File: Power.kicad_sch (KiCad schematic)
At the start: 34 parts, among them Q50 DMP3068L-7, SW50 SW_SPST, U50 MCP73831-2-OT, U51 MIC845H, U52 LM66200DRLR, U53 TPS631000DRLR

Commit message: Ground Stitching, PMOS 0-Res Moved,
DRC should be near cleared. Might want to reconsider mapping some pin functions? SD card detect line, also battery checker (making use of comparator). Also, double check if audio IC microphone pins (and ADC) are supposed to be pulled to VMID
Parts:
- C54, C55: footprint Capacitor_SMD:C_0603_1608Metric_Pad1.08x0.95mm_HandSolder -> Capacitor_SMD:C_0805_2012Metric
- TP50, TP52: footprint TestPoint:TestPoint_Pad_1.5x1.5mm -> footprints:TestPoint_Pad_1.5x1.5mm
- TP51: footprint TestPoint:TestPoint_Pad_1.5x1.5mm -> TestPoint:TestPoint_THTPad_1.5x1.5mm_Drill0.7mm
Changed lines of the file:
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@@
 			)
 		)
-		(property "Footprint" "TestPoint:TestPoint_Pad_1.5x1.5mm"
+		(property "Footprint" "footprints:TestPoint_Pad_1.5x1.5mm"
 			(at 55.88 31.75 0)
 			(effects
@@
 			)
 		)
-		(property "Footprint" "TestPoint:TestPoint_Pad_1.5x1.5mm"
+		(property "Footprint" "footprints:TestPoint_Pad_1.5x1.5mm"
 			(at 167.64 115.57 0)
 			(effects
@@
 			)
 		)
-		(property "Footprint" "Capacitor_SMD:C_0603_1608Metric_Pad1.08x0.95mm_HandSolder"
+		(property "Footprint" "Capacitor_SMD:C_0805_2012Metric"
 			(at 176.53 123.19 0)
 			(effects
@@
 			)
 		)
-		(property "Footprint" "TestPoint:TestPoint_Pad_1.5x1.5mm"
+		(property "Footprint" "TestPoint:TestPoint_THTPad_1.5x1.5mm_Drill0.7mm"
 			(at 46.99 66.04 0)
 			(effects
@@
 			)
 		)
-		(property "Footprint" "Capacitor_SMD:C_0603_1608Metric_Pad1.08x0.95mm_HandSolder"
+		(property "Footprint" "Capacitor_SMD:C_0805_2012Metric"
 			(at 252.73 123.19 0)
 			(effects

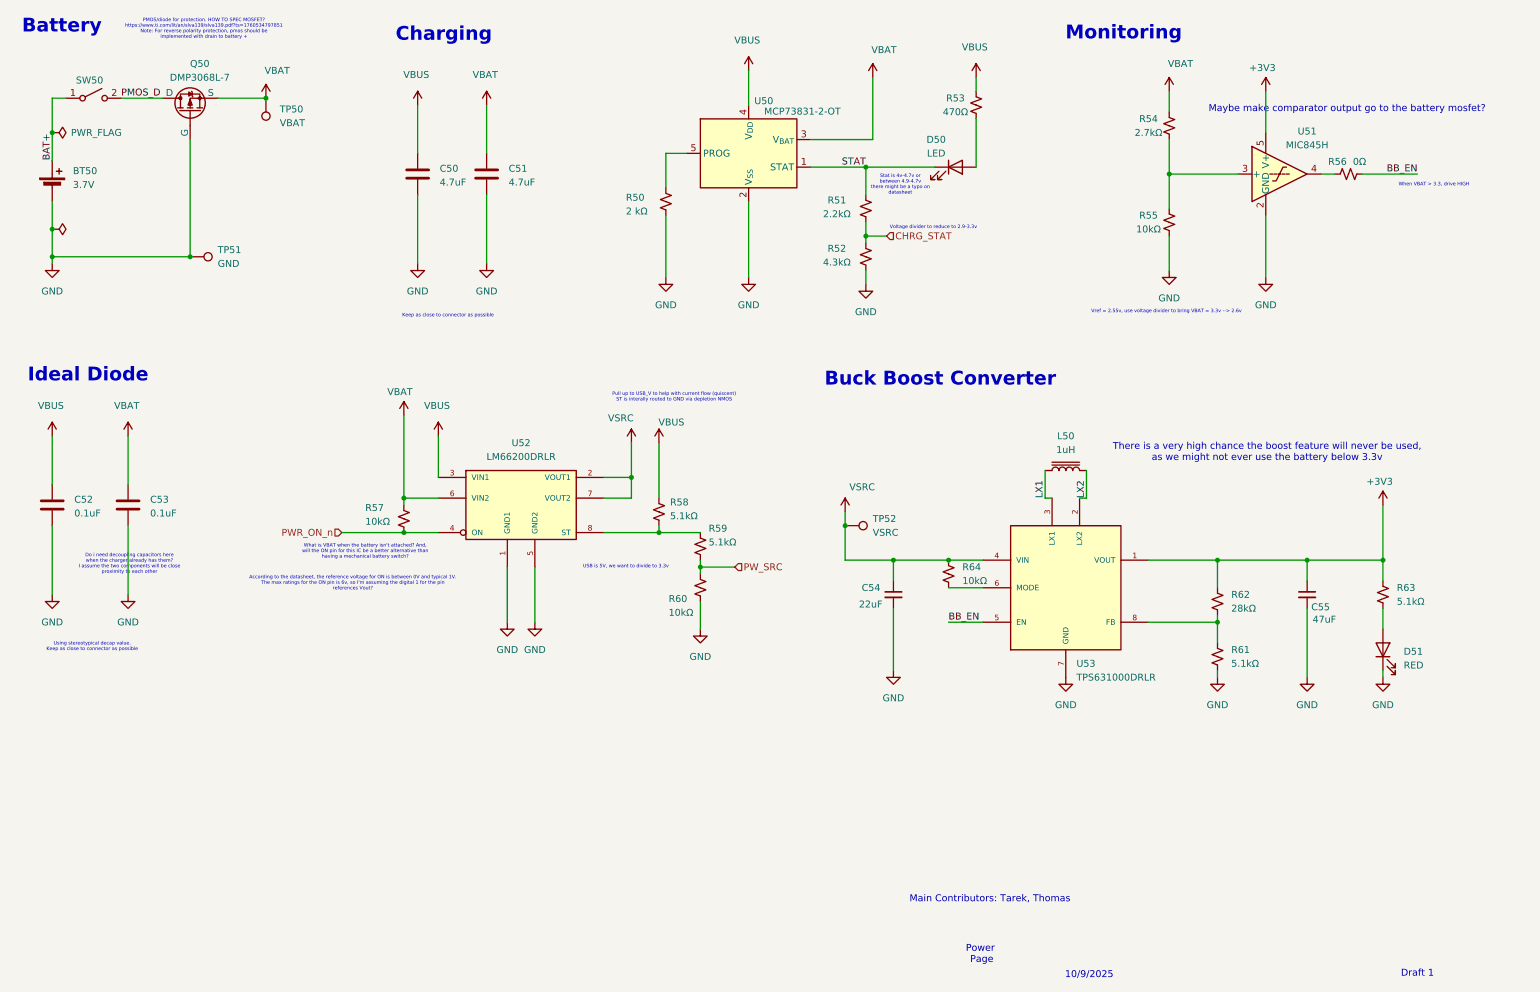
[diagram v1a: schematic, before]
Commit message: UNFINISHED: Rerouted Traces, new LEDs, replaced components
Removed charging status and power source signals from MCU and gave them their own LEDs. Added analog battery voltage and card detect as replacement. Also found out not all components are in stock... troubling to find replacements :( should have done this during schematic
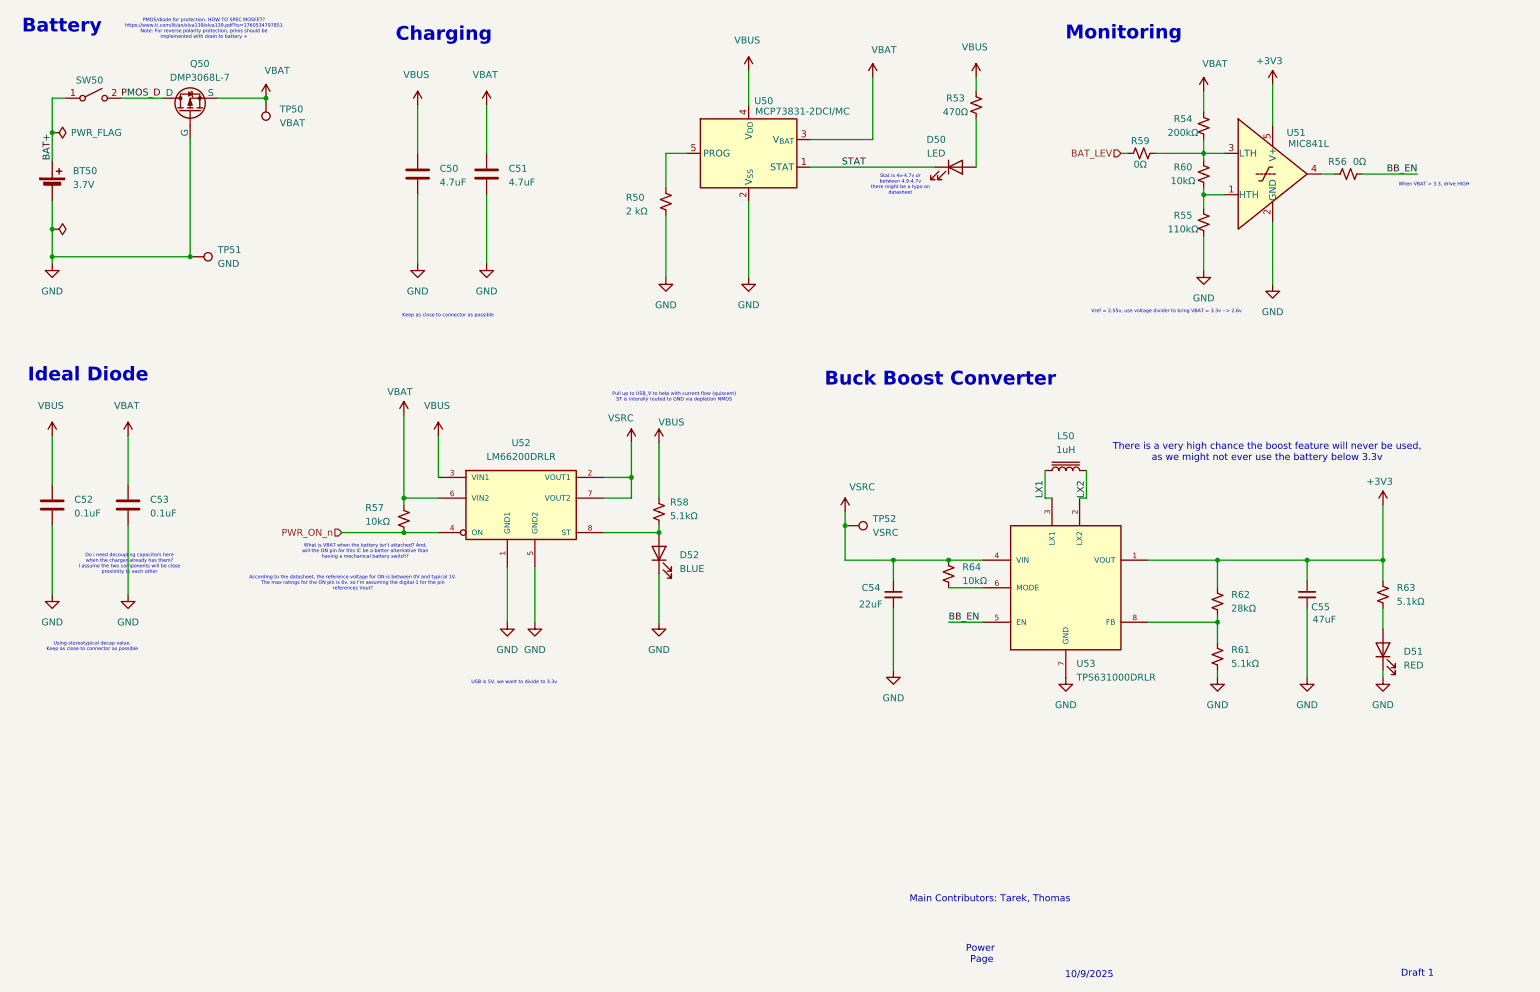
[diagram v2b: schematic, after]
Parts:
- removed R51: 2.2kΩ, Resistor_SMD:R_0603_1608Metric_Pad0.98x0.95mm_HandSolder, symbol Device:R_Small_US
- removed R52: 4.3kΩ, Resistor_SMD:R_0603_1608Metric_Pad0.98x0.95mm_HandSolder, symbol Device:R_Small_US
- added D52: BLUE, LED_SMD:LED_0603_1608Metric, symbol Device:LED
- R54: value 2.7kΩ -> 200kΩ
- R55: value 10kΩ -> 110kΩ
- R59: value 5.1kΩ -> 0Ω
- U50: value MCP73831-2-OT -> MCP73831-2DCI/MC
- U51: value MIC845H -> MIC841L
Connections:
- net GND: now also D52.1 (K); no longer R60.1
- net at R58.2, U52.8 (ST): now also D52.2 (A); no longer R59.1
- net at U51.1 (NIC): now also R55.2, R60.1
- net at R54.1, U51.3 (LTH): now also R59.1, R60.2; no longer R55.2
- net PW_SRC renamed BAT_LEV
- net BAT_LEV: no longer R60.2
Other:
- note removed: "Maybe make comparator output go to the battery mosfet?"
- note removed: "Voltage divider to reduce to 2.9-3.3v"
- moved on the sheet: R54, R55

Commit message: ORDERED: Updated Footprints, Silk Screen, Mounting Holes
Minor changes. This is the version sent to JLC
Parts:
- D50: footprint LED_SMD:LED_0805_2012Metric_Pad1.15x1.40mm_HandSolder -> LED_SMD:LED_0603_1608Metric
- L50: value 1uH -> DFE252012P-1R0M=P2; footprint Inductor_SMD:L_0805_2012Metric_Pad1.05x1.20mm_HandSolder -> Inductor_SMD:L_1008_2520Metric
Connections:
- net at U51.1 (NIC): now also R55.2, R60.1
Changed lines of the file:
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@@
 			)
 		)
-		(property "Footprint" "LED_SMD:LED_0805_2012Metric_Pad1.15x1.40mm_HandSolder"
+		(property "Footprint" "LED_SMD:LED_0603_1608Metric"
 			(at 187.96 44.45 0)
 			(effects
@@
 			)
 		)
-		(property "Value" "1uH"
+		(property "Value" "DFE252012P-1R0M=P2"
 			(at 208.28 96.52 90)
 			(effects
@@
 			)
 		)
-		(property "Footprint" "Inductor_SMD:L_0805_2012Metric_Pad1.05x1.20mm_HandSolder"
+		(property "Footprint" "Inductor_SMD:L_1008_2520Metric"
 			(at 208.28 100.33 0)
 			(effects
